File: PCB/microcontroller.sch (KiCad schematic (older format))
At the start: 6 parts, among them U1 DEV_KIT_EK-TM4C123GXL, U4 MC14504B

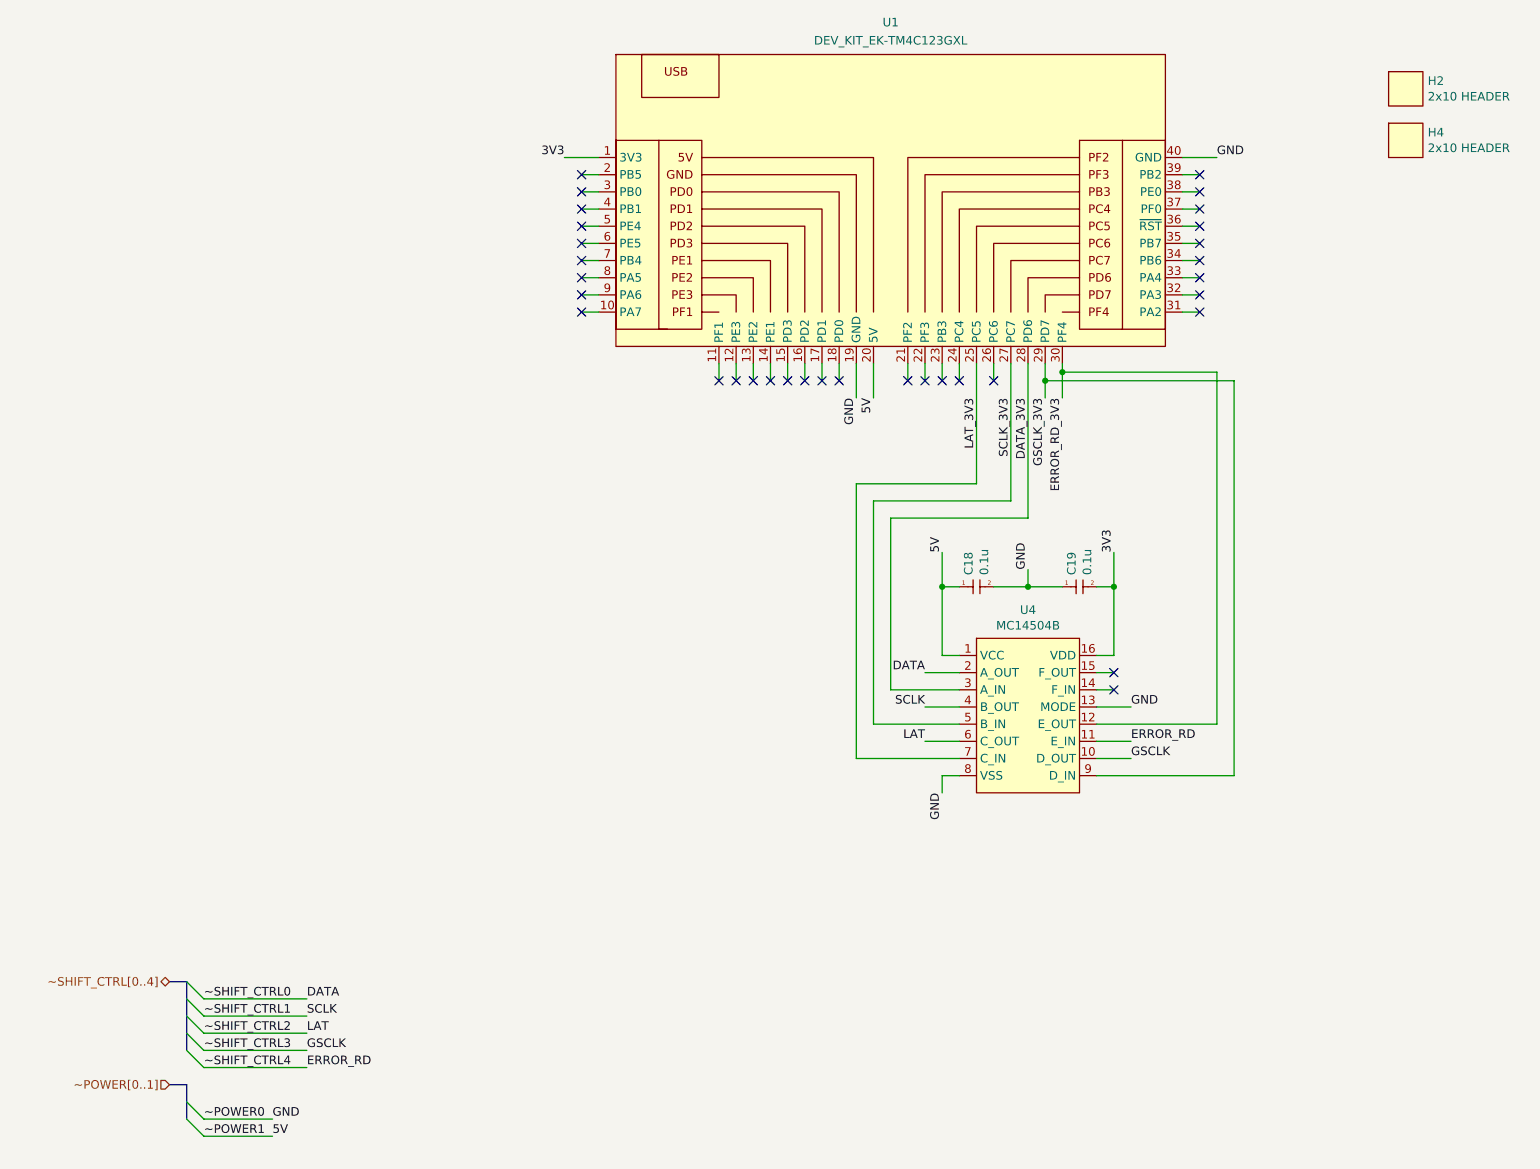
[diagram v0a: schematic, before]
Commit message: Removed Level Shifter, Cleaned up gerbers
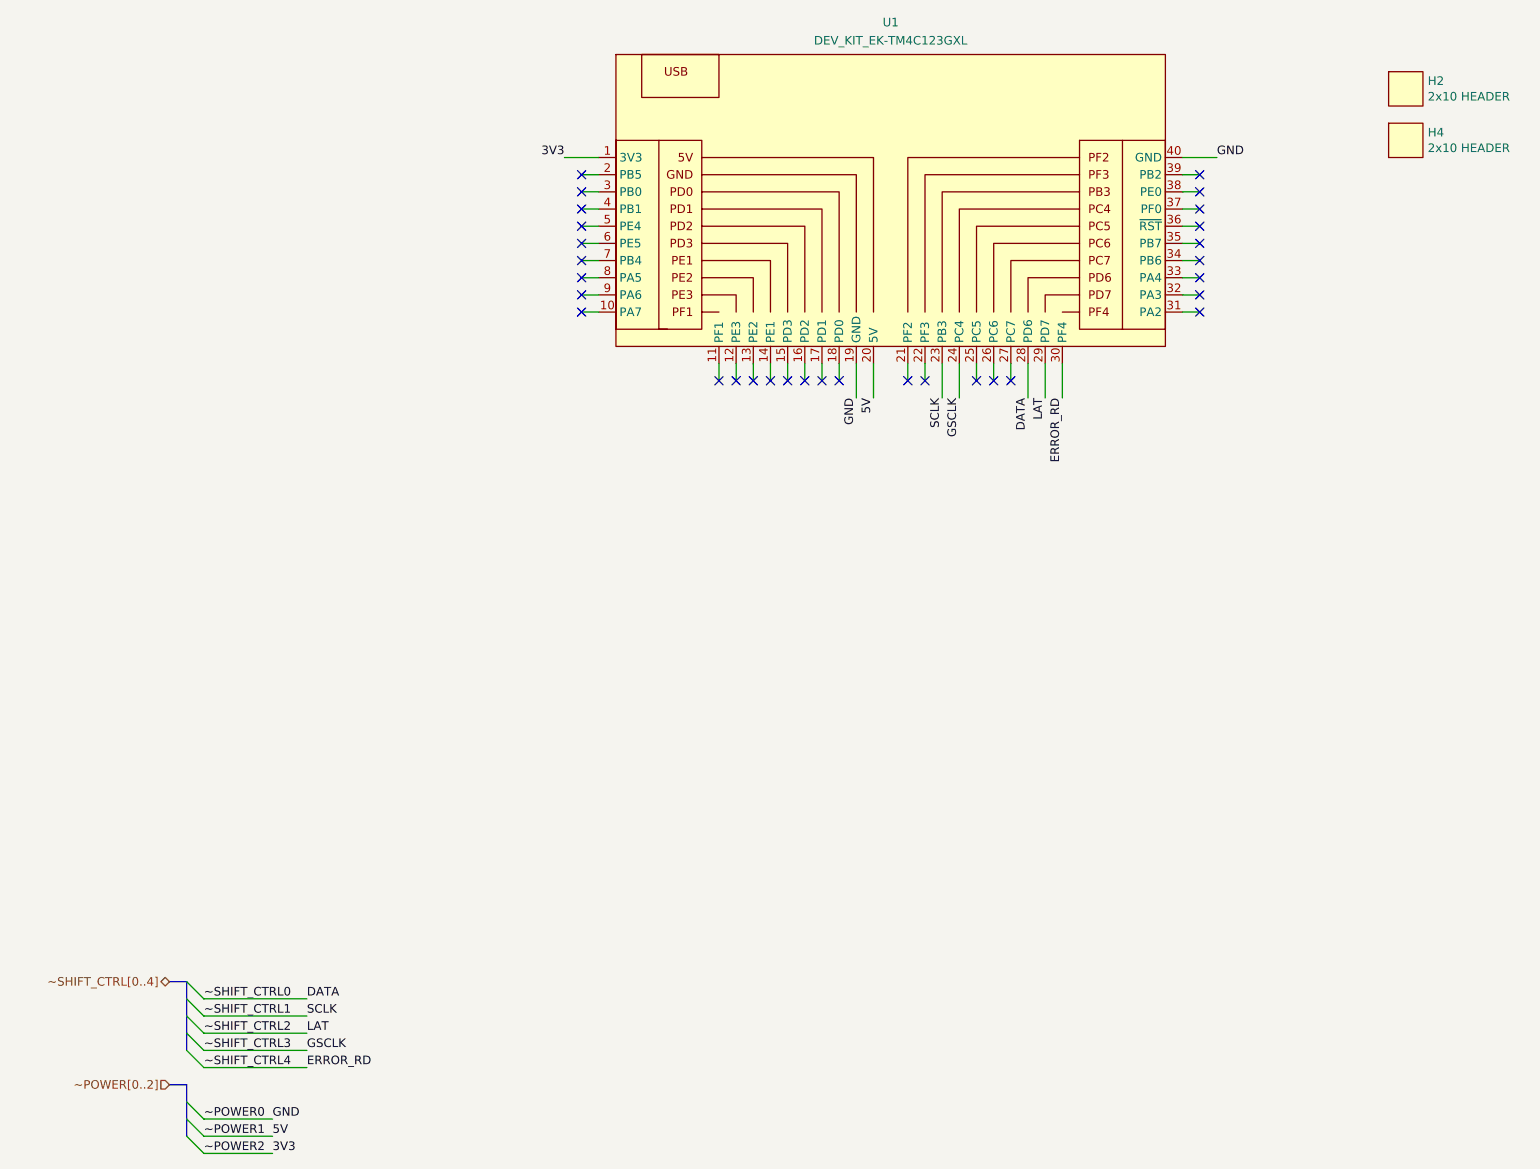
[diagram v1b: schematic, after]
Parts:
- removed C18, C19: 0.1u, local:SMD-0805, symbol Capacitor
- removed U4: MC14504B, local:SOIC-16, symbol MC14504B
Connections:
- net DATA_3V3 is gone; now on net DATA: U1.28 (PD6)
- net ERROR_RD_3V3 is gone; now on net ERROR_RD: U1.30 (PF4)
- net GSCLK_3V3 is gone; now on net LAT: U1.29 (PD7)
- net GSCLK: now also U1.24 (PC4)
- net SCLK: now also U1.23 (PB3)
- net LAT_3V3: no longer names the net of U1.25 (PC5)
- net SCLK_3V3: no longer names the net of U1.27 (PC7)
- no-connect marks 33 -> 31
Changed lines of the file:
@@
 Sheet 3 20
 Title "Christmas Tree Disco"
-Date "2017-08-15"
+Date "2017-08-23"
 Rev "V1.0"
 Comp "www.GitHub.com/Cryochasm"
@@
 $EndComp
 Text HLabel 1300 7500 0    50   Input ~ 0
-~~POWER[0..1]
+~~POWER[0..2]
 Wire Bus Line
 	1300 7500 1400 7500
 Wire Bus Line
-	1400 7500 1400 7700
+	1400 7500 1400 7800
 Entry Wire Line
 	1400 7600 1500 7700
@@
 	1    0    0    -1
 $EndComp
-$Comp
-L MC14504B U4
-U 1 1 5984BDBB
-P 6300 5300
-F 0 "U4" H 6300 5865 50  0000 C CNN
-F 1 "MC14504B" H 6300 5774 50  0000 C CNN
-F 2 "local:SOIC-16" H 6200 5800 50  0001 C CNN
-F 3 "http://www.onsemi.com/pub/Collateral/MC14504B-D.PDF" H 6300 6000 50  0001 C CNN
-F 4 "MC14504BDG" H 6300 6300 50  0001 C CNN "MPN"
-F 5 "Voltage Level Translator Unidirectional Circuit 6 Channel 16-SOIC" H 6300 6100 50  0001 C CNN "Description"
-F 6 "Yes" H 6300 6200 50  0001 C CNN "Included in BOM"
-	1    6300 5300
-	1    0    0    -1
-$EndComp
-Text Label 6800 4400 1    50   ~ 0
-3V3
-Text Label 5700 5100 2    50   ~ 0
-DATA
-Text Label 5700 5300 2    50   ~ 0
-SCLK
-Text Label 5700 5500 2    50   ~ 0
-LAT
-Text Label 6900 5600 0    50   ~ 0
-GSCLK
-Text Label 6900 5500 0    50   ~ 0
-ERROR_RD
-Wire Wire Line
-	5800 5000 5900 5000
-Wire Wire Line
-	5800 4400 5800 5000
-Text Label 5800 4400 1    50   ~ 0
-5V
-Wire Wire Line
-	5900 5700 5800 5700
-Wire Wire Line
-	5800 5700 5800 5800
-Text Label 5800 5800 3    50   ~ 0
-GND
-Wire Wire Line
-	5700 5100 5900 5100
-Wire Wire Line
-	5700 5300 5900 5300
-Wire Wire Line
-	5700 5500 5900 5500
-Wire Wire Line
-	6900 5500 6700 5500
-Wire Wire Line
-	6900 5600 6700 5600
 Text Label 3600 2100 2    50   ~ 0
 3V3
@@
 	3800 2100 3600 2100
 Wire Wire Line
-	6800 5000 6700 5000
-Wire Wire Line
-	6800 4400 6800 5000
-Wire Wire Line
-	6700 5100 6800 5100
-Wire Wire Line
-	6700 5200 6800 5200
-Wire Wire Line
-	6700 5400 7400 5400
-NoConn ~ 6800 5100
-NoConn ~ 6800 5200
-Wire Wire Line
 	6500 3300 6500 3500
-Wire Wire Line
-	7500 3400 7500 5700
-Wire Wire Line
-	7500 5700 6700 5700
-Wire Wire Line
-	5900 5200 5500 5200
-Wire Wire Line
-	5500 5200 5500 4200
-Wire Wire Line
-	5900 5400 5400 5400
-Wire Wire Line
-	5400 5400 5400 4100
-Wire Wire Line
-	5900 5600 5300 5600
-Wire Wire Line
-	5300 5600 5300 4000
 Wire Wire Line
 	3800 2200 3700 2200
@@
 	5700 3300 5700 3400
 Wire Wire Line
-	5800 3300 5800 3400
-Wire Wire Line
-	5900 3300 5900 3400
-Wire Wire Line
-	6000 3300 6000 4000
+	5800 3300 5800 3500
+Wire Wire Line
+	5900 3300 5900 3500
 Wire Wire Line
 	6100 3300 6100 3400
@@
 NoConn ~ 5600 3400
 NoConn ~ 5700 3400
-NoConn ~ 5800 3400
-NoConn ~ 5900 3400
 NoConn ~ 7300 3000
 NoConn ~ 6100 3400
-Wire Wire Line
-	6700 5300 6900 5300
-Text Label 6900 5300 0    50   ~ 0
-GND
-$Comp
-L Capacitor C18
-U 1 1 59876312
-P 6000 4600
-F 0 "C18" V 5954 4668 50  0000 L CNN
-F 1 "0.1u" V 6045 4668 50  0000 L CNN
-F 2 "local:SMD-0805" H 6000 4600 60  0001 C CNN
-F 3 "http://www.samsungsem.com/kr/support/library/product-catalog/mlcc.jsp" H 6000 4600 60  0001 C CNN
-F 4 "CL21B104KACWPNC" H 6000 4600 60  0001 C CNN "MPN"
-F 5 "0.1µF ±10% 25V Ceramic Capacitor X7R 0805 (2012 Metric)" H 6000 4600 60  0001 C CNN "Description"
-F 6 "Yes" H 6000 4600 60  0001 C CNN "Included in BOM"
-	1    6000 4600
-	1    0    0    -1
-$EndComp
-Wire Wire Line
-	5900 4600 5800 4600
-Connection ~ 5800 4600
-Wire Wire Line
-	6100 4600 6500 4600
-Wire Wire Line
-	6700 4600 6800 4600
-Connection ~ 6800 4600
-Wire Wire Line
-	6300 4600 6300 4500
-Connection ~ 6300 4600
-Text Label 6300 4500 1    50   ~ 0
-GND
+Text Label 5900 3500 3    50   ~ 0
+GSCLK
+Text Label 6500 3500 3    50   ~ 0
+ERROR_RD
+Text Label 6300 3500 3    50   ~ 0
+DATA
+Text Label 5800 3500 3    50   ~ 0
+SCLK
 Text Label 6400 3500 3    50   ~ 0
-GSCLK_3V3
-Text Label 6500 3500 3    50   ~ 0
-ERROR_RD_3V3
-Text Label 6300 3500 3    50   ~ 0
-DATA_3V3
-Text Label 6200 3500 3    50   ~ 0
-SCLK_3V3
-Text Label 6000 3500 3    50   ~ 0
-LAT_3V3
-$Comp
-L Capacitor C19
-U 1 1 59890F4A
-P 6600 4600
-F 0 "C19" V 6554 4668 50  0000 L CNN
-F 1 "0.1u" V 6645 4668 50  0000 L CNN
-F 2 "local:SMD-0805" H 6600 4600 60  0001 C CNN
-F 3 "http://www.samsungsem.com/kr/support/library/product-catalog/mlcc.jsp" H 6600 4600 60  0001 C CNN
-F 4 "CL21B104KACWPNC" H 6600 4600 60  0001 C CNN "MPN"
-F 5 "0.1µF ±10% 25V Ceramic Capacitor X7R 0805 (2012 Metric)" H 6600 4600 60  0001 C CNN "Description"
-F 6 "Yes" H 6600 4600 60  0001 C CNN "Included in BOM"
-	1    6600 4600
-	1    0    0    -1
-$EndComp
+LAT
 Wire Wire Line
 	6400 3300 6400 3500
 Wire Wire Line
-	6400 3400 7500 3400
-Connection ~ 6400 3400
-Wire Wire Line
-	6500 3350 7400 3350
-Connection ~ 6500 3350
-Wire Wire Line
-	7400 3350 7400 5400
-Wire Wire Line
-	6300 3300 6300 4200
-Wire Wire Line
-	6300 4200 5500 4200
-Wire Wire Line
-	6200 3300 6200 4100
-Wire Wire Line
-	6200 4100 5400 4100
-Wire Wire Line
-	6000 4000 5300 4000
+	6300 3300 6300 3500
 Wire Wire Line
 	7300 3000 7200 3000
+Text Label 1900 7900 0    50   ~ 0
+3V3
+Entry Wire Line
+	1400 7800 1500 7900
+Wire Wire Line
+	1500 7900 1900 7900
+Text Label 1500 7900 0    50   ~ 0
+~~POWER2
+Wire Wire Line
+	6200 3300 6200 3400
+Wire Wire Line
+	6000 3300 6000 3400
+NoConn ~ 6200 3400
+NoConn ~ 6000 3400
 $EndSCHEMATC

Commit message: Schematic V2
REQUIRES CHANGE TO SOFTWARE: Changed pin of LAT from D7 to D0 to avoid
using the non-maskable interrupt pin.

Added a SMD LED D8 to provide and enviornmental lighting effect.

Removed power supply circuit; USB power from the dev board is sufficent
for
LED brightness. Must be plugged into USB 3.0 or a 2A rated supply.

Updated symbol library to use KiBOM and to Lib Version 4.

TODO: Update  PCB
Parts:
- H2, H4: symbol Generic -> local:Generic; Config (none) -> Fit; Included in BOM Yes -> (none)
- U1: symbol DEV_KIT_EK-TM4C123GXL -> local:DEV_KIT_EK-TM4C123GXL; Config (none) -> Fit; Included in BOM No -> (none)
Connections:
- net ERROR_RD: now also U1.27 (PC7); no longer U1.30 (PF4)
- net LAT: now also U1.18 (PD0); no longer U1.29 (PD7)
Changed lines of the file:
@@
-EESchema Schematic File Version 2
+EESchema Schematic File Version 4
 LIBS:local
 LIBS:Christmas_Tree_Disco-cache
@@
 $Descr A 11000 8500
 encoding utf-8
-Sheet 3 20
+Sheet 3 19
 Title "Christmas Tree Disco"
-Date "2017-09-10"
-Rev "V1.1"
+Date "2017-09-20"
+Rev "V2"
 Comp "www.GitHub.com/Cryochasm"
 Comment1 ""
@@
 $EndDescr
 $Comp
-L DEV_KIT_EK-TM4C123GXL U1
+L local:DEV_KIT_EK-TM4C123GXL U1
 U 1 1 59812138
 P 5500 2500
@@
 F 4 "EK-TM4C123GXL" H 5500 2500 60  0001 C CNN "MPN"
 F 5 "Development Boards & Kits - ARM TIVA LaunchPAD" H 5500 2500 60  0001 C CNN "Description"
-F 6 "No" H 5500 2500 60  0001 C CNN "Included in BOM"
+F 6 "Fit" H 5500 2500 60  0001 C CNN "Config"
 	1    5500 2500
 	1    0    0    -1
@@
 Text Label 7400 2100 0    50   ~ 0
 GND
-Text Label 5400 3500 3    50   ~ 0
+Text Label 5400 4400 3    50   ~ 0
 5V
 Wire Wire Line
-	5400 3300 5400 3500
+	5400 3300 5400 4400
 Wire Wire Line
 	5300 3300 5300 3500
@@
 GND
 $Comp
-L Generic H2
+L local:Generic H2
 U 1 1 5984BC75
 P 8500 1700
@@
 F 4 "0015912200" H 8500 1400 50  0001 C CNN "MPN"
 F 5 "20 Positions Header, Breakaway Connector 0.100\" (2.54mm) Surface Mount Tin" H 8500 1300 50  0001 C CNN "Description"
-F 6 "Yes" H 8500 1200 50  0001 C CNN "Included in BOM"
+F 6 "Fit" H 8500 1200 50  0001 C CNN "Config"
 	1    8500 1700
 	1    0    0    -1
 $EndComp
 $Comp
-L Generic H4
+L local:Generic H4
 U 1 1 5984BD4E
 P 8500 2000
@@
 F 4 "0015912200" H 8500 1700 50  0001 C CNN "MPN"
 F 5 "20 Positions Header, Breakaway Connector 0.100\" (2.54mm) Surface Mount Tin" H 8500 1600 50  0001 C CNN "Description"
-F 6 "Yes" H 8500 1500 50  0001 C CNN "Included in BOM"
+F 6 "Fit" H 8500 1500 50  0001 C CNN "Config"
 	1    8500 2000
 	1    0    0    -1
@@
 	3800 2100 3600 2100
 Wire Wire Line
-	6500 3300 6500 3500
+	6500 3300 6500 3400
 Wire Wire Line
 	3800 2200 3700 2200
@@
 	5100 3300 5100 3400
 Wire Wire Line
-	5200 3300 5200 3400
+	5200 3300 5200 3500
 NoConn ~ 4500 3400
 NoConn ~ 4600 3400
@@
 NoConn ~ 5000 3400
 NoConn ~ 5100 3400
-NoConn ~ 5200 3400
 NoConn ~ 5600 3400
 NoConn ~ 5700 3400
@@
 Text Label 5900 3500 3    50   ~ 0
 GSCLK
-Text Label 6500 3500 3    50   ~ 0
+Text Label 6200 3500 3    50   ~ 0
 ERROR_RD
 Text Label 6300 3500 3    50   ~ 0
@@
 Text Label 5800 3500 3    50   ~ 0
 SCLK
-Text Label 6400 3500 3    50   ~ 0
+Text Label 5200 3500 3    50   ~ 0
 LAT
 Wire Wire Line
-	6400 3300 6400 3500
+	6400 3300 6400 3400
 Wire Wire Line
 	6300 3300 6300 3500
@@
 ~~POWER2
 Wire Wire Line
-	6200 3300 6200 3400
+	6200 3300 6200 3500
 Wire Wire Line
 	6000 3300 6000 3400
-NoConn ~ 6200 3400
 NoConn ~ 6000 3400
+NoConn ~ 6400 3400
+NoConn ~ 6500 3400
+$Comp
+L local:PWR_FLAG #P01
+U 1 1 5A202462
+P 5200 4300
+F 0 "#P01" H 5200 4450 50  0001 C CNN
+F 1 "PWR_FLAG" H 5278 4294 50  0000 L CNN
+F 2 "" H 5200 4300 50  0001 C CNN
+F 3 "" H 5200 4300 50  0001 C CNN
+	1    5200 4300
+	0    -1   -1   0
+$EndComp
+Wire Wire Line
+	5300 4300 5400 4300
+Connection ~ 5400 4300
 $EndSCHEMATC
